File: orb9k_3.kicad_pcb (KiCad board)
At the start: 2 copper layers, 49.5 x 33 mm, 27 parts, among them IC1 ADM232AARNZ, J1 DB9, P1 USB-C, P2 CONN_USBAUX, P3 Cortex_Debug, U1 ATSAMD21E18A_AU, U2 SPX3819M5, Y1 32.768khz

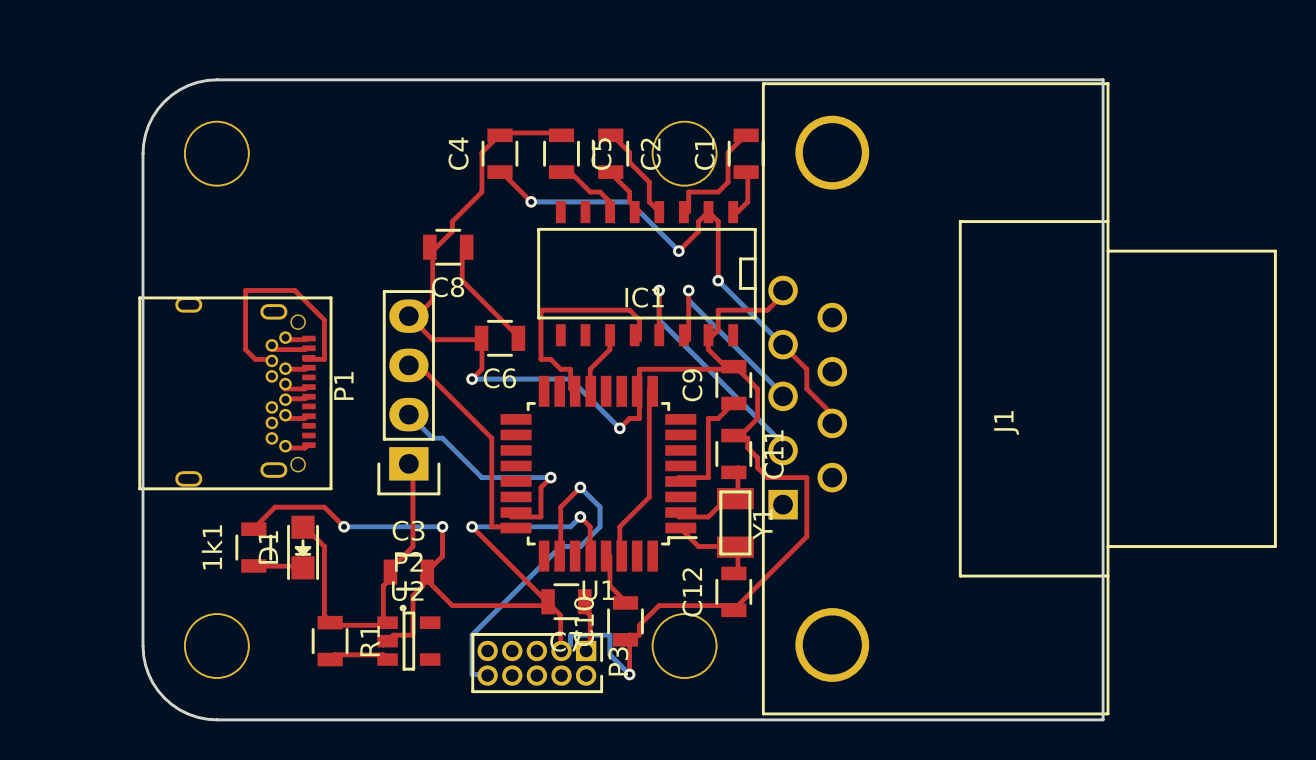
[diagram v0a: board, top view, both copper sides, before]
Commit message: screwed up prog connect; trying to fix
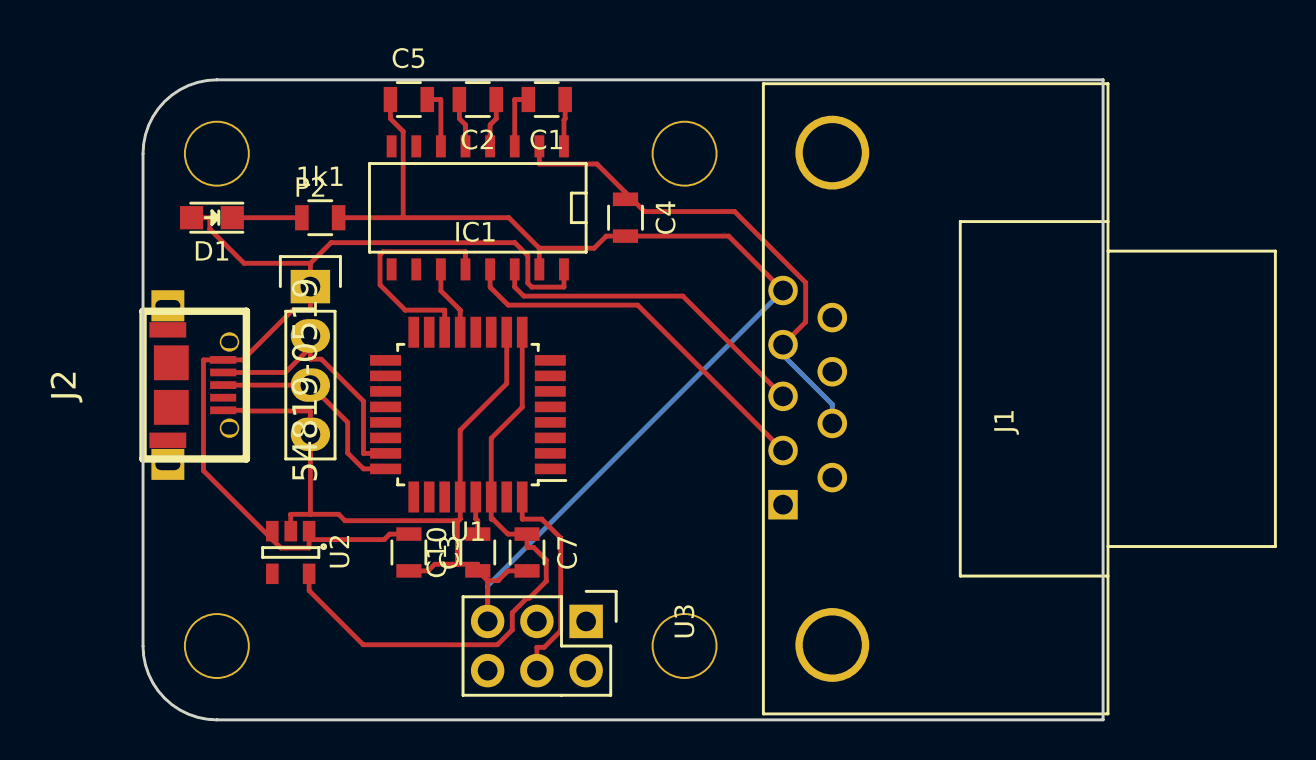
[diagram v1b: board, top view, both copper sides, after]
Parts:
- removed C11, C12: 22pf, Resistors_SMD:R_0805
- removed C6, C8: 10uf, Resistors_SMD:R_0805
- removed C9: 1uf, Resistors_SMD:R_0805
- removed P1: USB-C, thingotron:USB-C
- removed P3: Cortex_Debug, Pin_Headers:Pin_Header_Straight_2x05_Pitch1.27mm
- removed R1: 100k, Resistors_SMD:R_0805
- removed Y1: 32.768khz, thingotron:smdxtal_3.2x1.5
- added J2: 54819-0519, thing_custom:molex_microusb, F.Cu at (45.0, 91.7)
- added U3: 6-pin-atmel-ice, Pin_Headers:Pin_Header_Straight_2x03, F.Cu at (67.9, 103.9)
- C7: value 1uf -> 0.1uf
- moved D1 17.7 mm to (48.6, 83.1), turned to 180 degrees
- moved 1k1 17.4 mm to (54.1, 83.1), turned to 0 degrees
- moved C1 10.7 mm to (65.8, 77.0), turned to 180 degrees
- moved P2 10.5 mm to (53.6, 86.7), turned to 0 degrees
- moved IC1 9.37 mm to (62.3, 82.6)
- moved C10 8.41 mm to (62.3, 100.4)
- moved C5 8.36 mm to (58.7, 77.0), turned to 0 degrees
- moved U2 7.62 mm to (52.6, 100.4), turned to 270 degrees
- moved C2 7.41 mm to (62.3, 77.0), turned to 180 degrees
- moved U1 7.39 mm to (61.8, 93.3)
- moved C4 7.27 mm to (69.9, 83.1), turned to 270 degrees
- moved C7 3.25 mm to (64.8, 100.4), turned to 270 degrees
- moved C3 1.02 mm to (58.7, 100.4), turned to 270 degrees
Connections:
- U2 pad 3: Net-(R1-Pad2) -> VBUS
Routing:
- net GND: track 129.5 -> 97.4 mm, vias 7 -> 0
- net VBUS: track 20.3 -> 52.0 mm
- net RESET: track 18.7 -> 0.00 mm, vias 1 -> 0
- net Net-(P1-Pad3): track 12.9 -> 0.00 mm
- net +3V3: track 19.2 -> 31.6 mm
- net SWDIO: track 0.00 -> 11.1 mm
- net AREF: track 7.06 -> 0.00 mm
- net Net-(IC1-Pad14): track 10.8 -> 17.1 mm, vias 1 -> 0
- net Net-(U1-Pad2): track 5.87 -> 0.00 mm
- net Net-(IC1-Pad13): track 13.9 -> 19.5 mm, vias 1 -> 0
- net Net-(U1-Pad1): track 5.63 -> 0.00 mm
- net Net-(C1-Pad2): track 6.61 -> 3.11 mm
- net Net-(R1-Pad2): track 3.18 -> 0.00 mm
- net Net-(C2-Pad1): track 5.27 -> 2.54 mm
- net Net-(C4-Pad1): track 28.5 -> 26.3 mm, vias 3 -> 0
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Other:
- net class Default: clearance 0.15 -> 0.215; via_dia 0.6 -> 0.889; via_drill 0.4 -> 0.635
- rule trace_clearance: 0.15 -> 0.215

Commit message: first worked, 2/3 inop
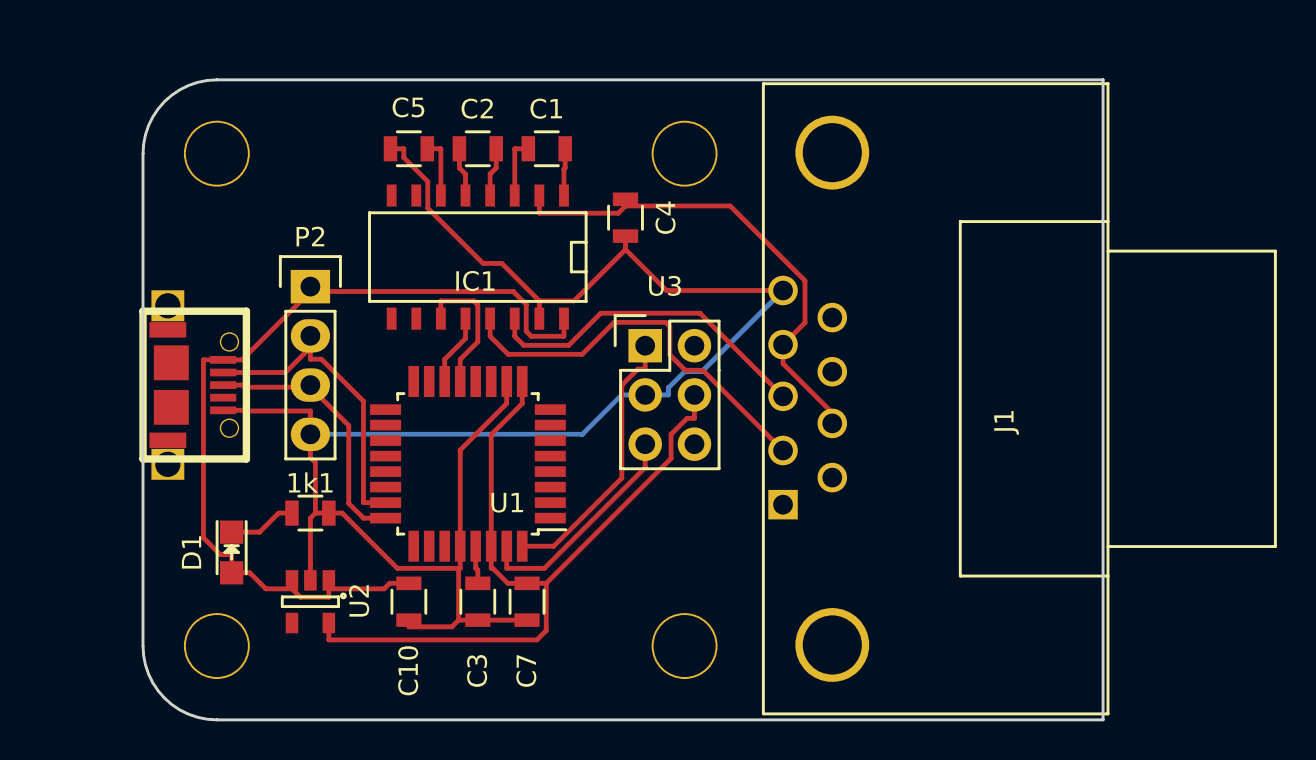
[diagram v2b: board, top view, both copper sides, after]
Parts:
- J2: value 54819-0519 -> WM17143CT-ND
- moved D1 17.3 mm to (49.6, 100.4), turned to 270 degrees
- moved 1k1 15.2 mm to (53.6, 98.4)
- moved U3 14.5 mm to (70.9, 89.7), turned to 0 degrees
- moved U2 2.74 mm to (53.6, 102.9)
- moved C10 2.54 mm to (62.3, 102.9)
- moved C3 2.54 mm to (58.7, 102.9)
- moved C7 2.54 mm to (64.8, 102.9)
- moved IC1 2.54 mm to (62.3, 85.1)
- moved C1 2.54 mm to (65.8, 79.6)
- moved C2 2.54 mm to (62.3, 79.6)
- moved C5 2.54 mm to (58.7, 79.6)
- moved U1 2.54 mm to (61.8, 95.8)
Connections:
- net AREF renamed Net-(U1-Pad4)
- net RESET renamed Net-(U1-Pad26)
- U3 pad 1: Net-(U3-Pad1) -> SWDIO
- U3 pad 3: Net-(U3-Pad3) -> GND
- U3 pad 4: SWDIO -> +3V3
- U3 pad 5: GND -> SWCLK
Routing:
- net SWCLK: track 0.00 -> 11.6 mm
- net +3V3: track 31.6 -> 41.3 mm
- net RX0: track 12.0 -> 3.69 mm
- net VBUS: track 52.0 -> 46.0 mm
- net TX0: track 3.66 -> 7.23 mm
- net SWDIO: track 11.1 -> 14.1 mm
- net D+: track 11.1 -> 13.7 mm
- net D-: track 13.7 -> 16.2 mm
- net Net-(IC1-Pad13): track 19.5 -> 20.7 mm
- net Net-(C4-Pad1): track 26.3 -> 25.6 mm

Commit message: prior to switching serial drivers
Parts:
- removed 1k1: R, Resistors_SMD:R_0805
- removed D1: Led_Small, LEDs:LED_0805
- moved C7 7.64 mm to (57.2, 103.4), turned to 90 degrees
- moved C3 7.22 mm to (53.1, 98.4), turned to 0 degrees
- moved U3 6.18 mm to (69.9, 95.8)
- moved C4 2.03 mm to (69.9, 85.1)
- moved U2 1.14 mm to (53.1, 101.9)
- moved C10 0.51 mm to (61.8, 102.9), turned to 0 degrees
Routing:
- net VBUS: track 46.0 -> 38.1 mm
- net SWDIO: track 14.1 -> 7.79 mm
- net +3V3: track 41.3 -> 35.7 mm
- net SWCLK: track 11.6 -> 7.40 mm
- net TX0: track 7.23 -> 3.66 mm
- net Net-(1k1-Pad1): track 3.52 -> 0.00 mm
- net RX0: track 3.69 -> 7.19 mm
- net Net-(IC1-Pad13): track 20.7 -> 18.5 mm
- net Net-(IC1-Pad14): track 17.4 -> 16.0 mm
- net Net-(C10-Pad2): track 1.97 -> 3.09 mm

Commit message: proto1!
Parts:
- removed IC1: ADM232AARNZ, SMD_Packages:SO-16-N
- added C6: 10uf, Resistors_SMD:R_0805, F.Cu at (53.1, 89.2)
- added C8: 10uf, Resistors_SMD:R_0805, F.Cu at (53.6, 79.6)
- added IC2: MAX3232, SMD_Packages:SO-16-N, F.Cu at (62.3, 85.1)
- added P1: USBV+D-, Pin_Headers:Pin_Header_Straight_2x01_Pitch2.54mm, F.Cu at (47.0, 83.1)
- added U4: TC1240A, TO_SOT_Packages_SMD:SOT-23-6_Handsoldering, F.Cu at (52.1, 84.6)
- J1: value DB9 -> DB9-PowerDTRRTS
- P2: value CONN_USBAUX -> USBD+GND; footprint Pin_Headers:Pin_Header_Straight_1x04 -> Pin_Headers:Pin_Header_Straight_2x01_Pitch2.54mm
- moved P2 16.6 mm to (47.0, 101.9), turned to 90 degrees
- moved U3 1.14 mm to (68.9, 95.3)
- moved U1 1.02 mm to (60.7, 95.8)
- moved J2 0.76 mm to (45.0, 92.5)
- moved C3 0.51 mm to (53.1, 97.8)
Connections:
- J1 pad 4: Net-(C4-Pad1) -> +10V
- J1 pad 7: Net-(C4-Pad1) -> +10V
- P2 pad 1: VBUS -> GND
- P2 pad 2: D- -> D+
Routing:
- net +10V: track 0.00 -> 43.1 mm
- net +3V3: track 35.7 -> 60.7 mm
- net Net-(C4-Pad1): track 25.2 -> 6.31 mm
- net Net-(C6-Pad1): track 0.00 -> 7.35 mm
- net VBUS: track 38.1 -> 33.6 mm
- net D+: track 13.7 -> 18.0 mm, vias 0 -> 1
- net Net-(C6-Pad2): track 0.00 -> 3.64 mm
- net D-: track 16.2 -> 19.4 mm, vias 0 -> 1
- net GND: track 97.6 -> 94.7 mm
- net Net-(IC2-Pad14): track 16.0 -> 18.3 mm
- net Net-(C10-Pad2): track 3.09 -> 3.92 mm
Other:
- board text added: "Orb9k3 Proto1"

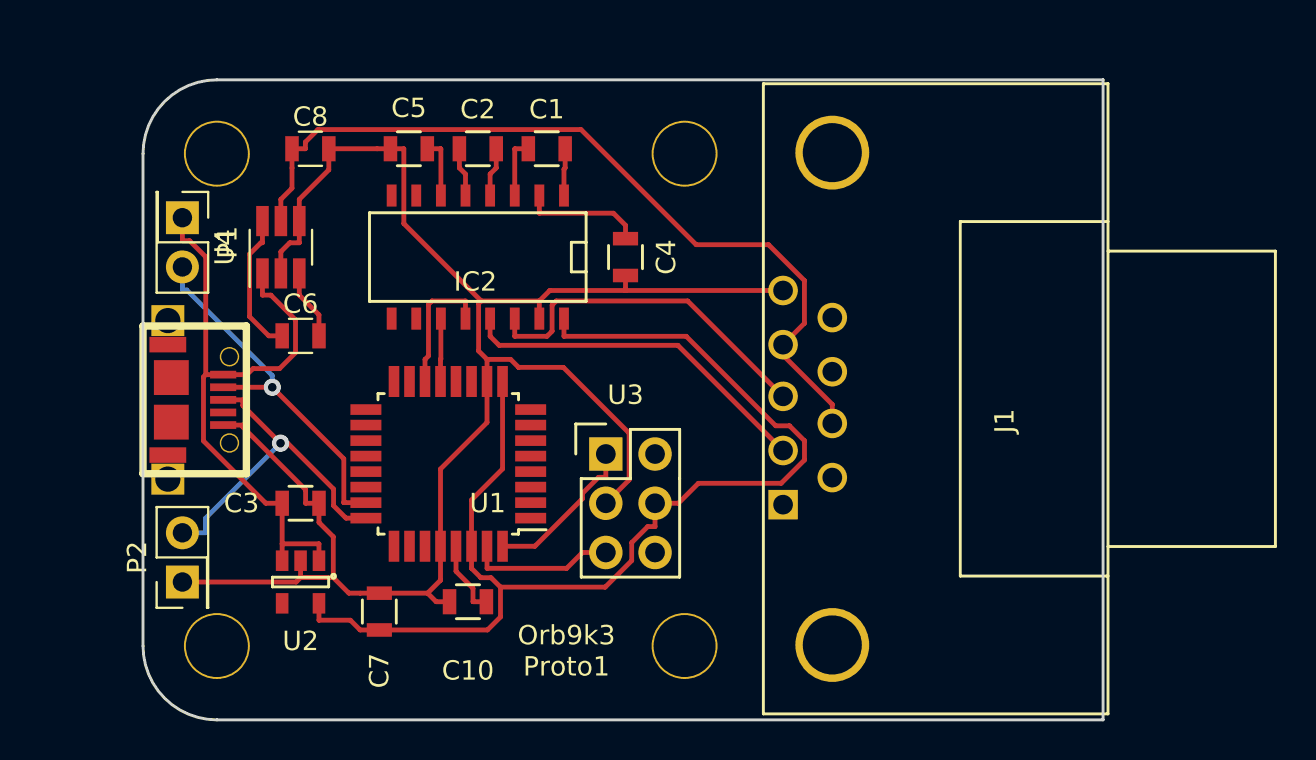
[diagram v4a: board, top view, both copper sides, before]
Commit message: converted schematics to use project lib orb9k_3.lib
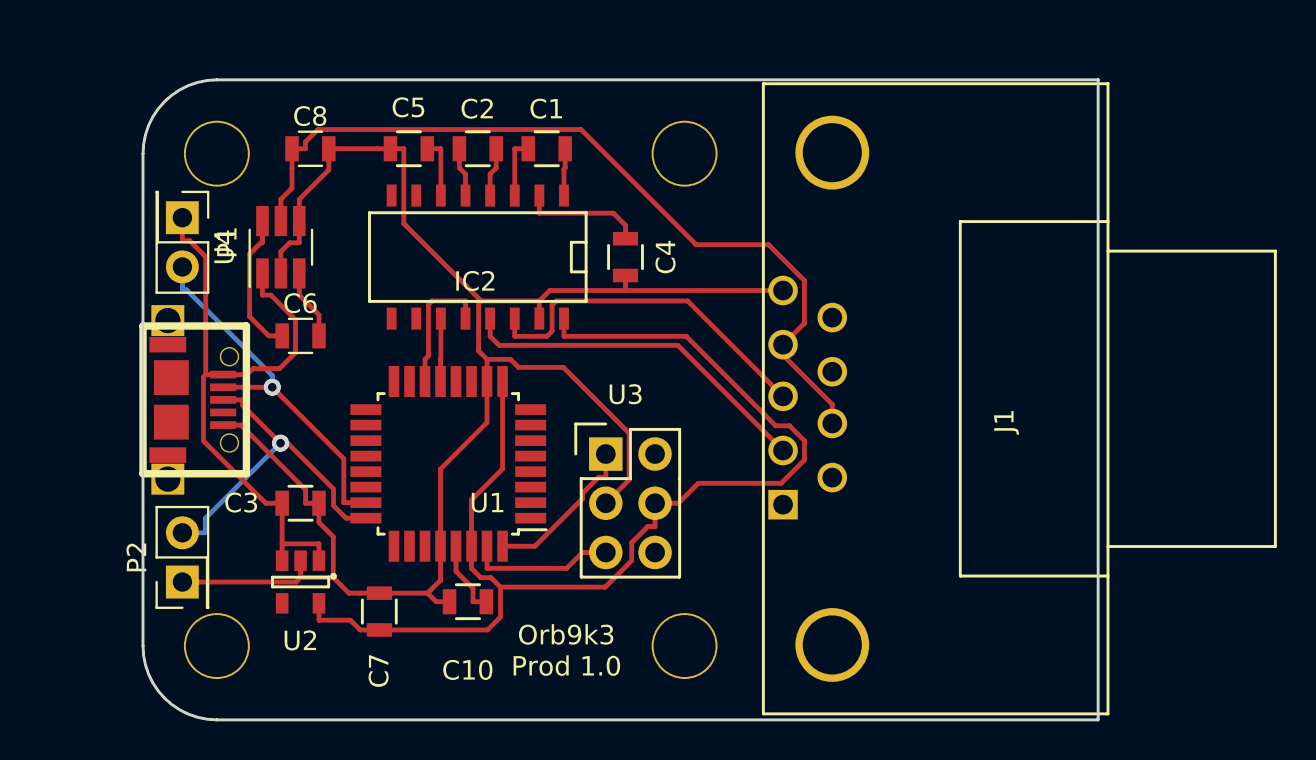
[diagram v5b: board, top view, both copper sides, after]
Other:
- board size 49.5 x 33 mm -> 49.3 x 33 mm
- board text added: "Orb9k3 Prod 1.0"
- board text removed: "Orb9k3 Proto1"
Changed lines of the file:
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@@
     (links 47)
     (no_connects 0)
-    (area 44.924999 75.924999 94.605001 109.095001)
+    (area 39.5018 73.5 103.710001 109.095001)
     (thickness 1.6)
-    (drawings 7)
+    (drawings 8)
     (tracks 207)
     (zones 0)
@@
     )
   )
-  (gr_text "Orb9k3\nProto1" (at 66.844 105.464) (layer F.SilkS)
+  (target plus (at 45 76) (size 5) (width 0.15) (layer Edge.Cuts))
+  (gr_text "Orb9k3\nProd 1.0" (at 66.844 105.464) (layer F.SilkS)
     (effects (font (size 1 1) (thickness 0.2)))
   )
   (gr_line (start 45 79.81) (end 45 105.21) (angle 90) (layer Edge.Cuts) (width 0.15))
-  (gr_line (start 94.53 109.02) (end 48.81 109.02) (angle 90) (layer Edge.Cuts) (width 0.15))
-  (gr_line (start 94.53 76) (end 94.53 109.02) (angle 90) (layer Edge.Cuts) (width 0.15))
-  (gr_line (start 48.81 76) (end 94.53 76) (angle 90) (layer Edge.Cuts) (width 0.15))
+  (gr_line (start 94.276012 109.02) (end 48.81 109.02) (angle 90) (layer Edge.Cuts) (width 0.15))
+  (gr_line (start 94.276012 76) (end 94.276012 109.02) (angle 90) (layer Edge.Cuts) (width 0.15))
+  (gr_line (start 48.81 76) (end 94.276012 76) (angle 90) (layer Edge.Cuts) (width 0.15))
   (gr_arc (start 48.81 105.21) (end 48.81 109.02) (angle 90) (layer Edge.Cuts) (width 0.15))
   (gr_arc (start 48.81 79.81) (end 45 79.81) (angle 90) (layer Edge.Cuts) (width 0.15))

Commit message: a few changes to catch up
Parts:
- added SW1: B3U-1000P, modules:SW_B3U-1000P, F.Cu at (61.8, 107.0)
- J2: footprint thing_custom:molex_microusb -> modules:FCI_10103594-0001LF
- moved J2 1.78 mm to (46.8, 92.5), turned to 270 degrees
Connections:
- IC2 pad 10: Net-(IC2-Pad10) -> (no net)
- IC2 pad 7: Net-(IC2-Pad7) -> (no net)
- IC2 pad 8: Net-(IC2-Pad8) -> (no net)
- IC2 pad 9: Net-(IC2-Pad9) -> (no net)
- J1 pad 1: Net-(J1-Pad1) -> (no net)
- J1 pad 6: Net-(J1-Pad6) -> (no net)
- J1 pad 8: Net-(J1-Pad8) -> (no net)
- J1 pad 9: Net-(J1-Pad9) -> (no net)
- J2 pad 4: Net-(J2-Pad4) -> (no net)
- U1 pad 1: Net-(U1-Pad1) -> (no net)
- U1 pad 11: Net-(U1-Pad11) -> (no net)
- U1 pad 12: Net-(U1-Pad12) -> (no net)
- U1 pad 15: Net-(U1-Pad15) -> (no net)
- U1 pad 16: Net-(U1-Pad16) -> (no net)
- U1 pad 17: Net-(U1-Pad17) -> (no net)
- U1 pad 18: Net-(U1-Pad18) -> (no net)
- U1 pad 19: Net-(U1-Pad19) -> (no net)
- U1 pad 2: Net-(U1-Pad2) -> (no net)
- U1 pad 20: Net-(U1-Pad20) -> (no net)
- U1 pad 21: Net-(U1-Pad21) -> (no net)
- U1 pad 22: Net-(U1-Pad22) -> (no net)
- U1 pad 25: Net-(U1-Pad25) -> (no net)
- U1 pad 27: Net-(U1-Pad27) -> (no net)
- U1 pad 3: Net-(U1-Pad3) -> (no net)
- U1 pad 4: Net-(U1-Pad4) -> (no net)
- U1 pad 5: Net-(U1-Pad5) -> (no net)
- U1 pad 6: Net-(U1-Pad6) -> (no net)
- U1 pad 7: Net-(U1-Pad7) -> (no net)
- U1 pad 8: Net-(U1-Pad8) -> (no net)
- U3 pad 2: Net-(U3-Pad2) -> (no net)
- U3 pad 6: Net-(U3-Pad6) -> (no net)
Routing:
- net GND: track 94.7 -> 107.7 mm
- net +3V3: track 60.7 -> 68.6 mm
- net Net-(SW1-Pad1): track 0.00 -> 7.90 mm
- net VBUS: track 33.6 -> 41.2 mm, vias 0 -> 1
- net Net-(J2-PadS1): track 0.00 -> 1.92 mm
- net D+: track 18.0 -> 19.7 mm
- net D-: track 19.4 -> 18.2 mm, vias 1 -> 0
